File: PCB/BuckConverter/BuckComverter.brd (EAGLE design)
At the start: 65 x 60 mm, 34 parts, among them IC1 LP2950CDT-3.3

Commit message: テストパッドを追加
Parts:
- added PAD1, PAD2, PAD3, PAD4: (no value), wirepad:1,6/0,8
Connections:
- net +12V: now also PAD2.1
- net GND: now also PAD1.1
- net IC_SIG_5V: now also PAD4.1
- net VA_IN: now also PAD3.1
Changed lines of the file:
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@@
 <?xml version="1.0" encoding="utf-8"?>
 <!DOCTYPE eagle SYSTEM "eagle.dtd">
-<eagle version="7.2.0">
+<eagle version="7.5.0">
 <drawing>
 <settings>
@@
 <layers>
 <layer number="1" name="Top" color="4" fill="1" visible="yes" active="yes"/>
+<layer number="2" name="Route2" color="1" fill="3" visible="no" active="no"/>
+<layer number="3" name="Route3" color="4" fill="3" visible="no" active="no"/>
+<layer number="14" name="Route14" color="1" fill="6" visible="no" active="no"/>
+<layer number="15" name="Route15" color="4" fill="6" visible="no" active="no"/>
 <layer number="16" name="Bottom" color="1" fill="1" visible="yes" active="yes"/>
 <layer number="17" name="Pads" color="2" fill="1" visible="yes" active="yes"/>
@@
 </element>
 <element name="ZD1" library="diode" package="DO34Z7" value="BZV10" x="61.595" y="24.13" rot="R270"/>
+<element name="PAD1" library="wirepad" package="1,6/0,8" value="" x="12.7" y="38.4175"/>
+<element name="PAD2" library="wirepad" package="1,6/0,8" value="" x="13.6525" y="26.3525"/>
+<element name="PAD3" library="wirepad" package="1,6/0,8" value="" x="55.88" y="31.4325"/>
+<element name="PAD4" library="wirepad" package="1,6/0,8" value="" x="44.45" y="45.72"/>
 </elements>
 <signals>
@@
 <wire x1="23.8125" y1="26.67" x2="23.8125" y2="28.575" width="0.6096" layer="16"/>
 <wire x1="19.685" y1="32.385" x2="18.7325" y2="28.575" width="1.016" layer="16"/>
+<contactref element="PAD2" pad="1"/>
 </signal>
 <signal name="GATE_SIG">
@@
 <wire x1="48.26" y1="6.985" x2="52.705" y2="2.54" width="0.4064" layer="16"/>
 <wire x1="52.705" y1="2.54" x2="60.0075" y2="2.54" width="0.4064" layer="16"/>
+<contactref element="PAD1" pad="1"/>
 </signal>
 <signal name="N$5">
@@
 <wire x1="44.45" y1="40.64" x2="44.45" y2="45.72" width="0.4064" layer="16"/>
 <wire x1="44.45" y1="45.72" x2="49.53" y2="46.99" width="0.4064" layer="16"/>
+<contactref element="PAD4" pad="1"/>
 </signal>
 <signal name="VA_IN">
@@
 <wire x1="54.75" y1="35.68" x2="54.61" y2="36.83" width="0.254" layer="16"/>
 <wire x1="54.75" y1="35.43" x2="54.61" y2="36.83" width="0.254" layer="16"/>
-<wire x1="55.88" y1="34.29" x2="55.88" y2="27.94" width="0.4064" layer="16"/>
+<wire x1="55.88" y1="34.29" x2="55.88" y2="33.9725" width="0.4064" layer="16"/>
+<wire x1="55.88" y1="31.4325" x2="55.88" y2="27.94" width="0.4064" layer="16"/>
 <wire x1="54.75" y1="35.43" x2="55.88" y2="34.29" width="0.4064" layer="16"/>
 <wire x1="54.61" y1="46.99" x2="54.61" y2="36.83" width="0.4064" layer="16"/>
@@
 <wire x1="59.055" y1="27.94" x2="61.2775" y2="28.2575" width="0.4064" layer="16"/>
 <wire x1="61.2775" y1="28.2575" x2="61.595" y2="27.94" width="0.4064" layer="16"/>
+<contactref element="PAD3" pad="1"/>
+<wire x1="55.88" y1="31.4325" x2="55.88" y2="33.9725" width="0.4064" layer="16"/>
 </signal>
 <signal name="N$4">

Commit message: 穴径を0.8, 1.0, 1.5, 3.2mmに統一
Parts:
- added PAD5: (no value), wirepad:1,6/0,8
- moved C_PAS_OUT 0.95 mm to (23.2, 44.5)
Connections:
- net VOUT: now also PAD5.1
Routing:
- net GND: track 331.3 -> 333.0 mm
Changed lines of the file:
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@@
 <element name="C_OUT" library="rcl" package="E2,5-7" value="100uF" x="18.0975" y="45.085" rot="R270"/>
 <element name="C_PAS_IN" library="rcl" package="C3216" value="0.1uF" x="9.2075" y="32.0675" rot="MR90"/>
-<element name="C_PAS_OUT" library="rcl" package="C3216" value="0.1uF" x="24.13" y="44.45" rot="MR270"/>
+<element name="C_PAS_OUT" library="rcl" package="C3216" value="0.1uF" x="23.1775" y="44.45" rot="MR270"/>
 <element name="C_REGIN" library="rcl" package="E2,5-6" value="10u" x="5.3975" y="15.5575" rot="R270"/>
 <element name="C_REGOUT" library="rcl" package="E2,5-6" value="10u" x="20.32" y="15.5575" rot="R270"/>
@@
 <element name="PAD3" library="wirepad" package="1,6/0,8" value="" x="55.88" y="31.4325"/>
 <element name="PAD4" library="wirepad" package="1,6/0,8" value="" x="44.45" y="45.72"/>
+<element name="PAD5" library="wirepad" package="1,6/0,8" value="" x="13.335" y="53.975"/>
 </elements>
 <signals>
@@
 <wire x1="26.67" y1="36.83" x2="26.67" y2="41.91" width="1.27" layer="16"/>
 <wire x1="26.67" y1="41.91" x2="26.035" y2="42.0975" width="1.27" layer="16"/>
-<wire x1="26.035" y1="42.0975" x2="24.13" y2="43.05" width="1.27" layer="16"/>
-<wire x1="24.26" y1="42.8625" x2="24.13" y2="43.05" width="1.27" layer="16"/>
+<wire x1="26.035" y1="42.0975" x2="23.1775" y2="43.05" width="1.27" layer="16"/>
+<wire x1="24.26" y1="42.8625" x2="23.1775" y2="43.05" width="1.27" layer="16"/>
 <wire x1="24.26" y1="42.8625" x2="19.05" y2="43.18" width="1.27" layer="16"/>
 <wire x1="52.07" y1="46.99" x2="52.07" y2="36.83" width="0.4064" layer="16"/>
@@
 <vertex x="30" y="36"/>
 <vertex x="30" y="42"/>
-<vertex x="29.175" y="43.1425"/>
+<vertex x="29.4925" y="43.7775"/>
 <vertex x="4.3175" y="45.365"/>
 </polygon>
@@
 <wire x1="5.2578" y1="48.26" x2="5.055" y2="48.2389" width="0.254" layer="16"/>
 <wire x1="5.2578" y1="48.26" x2="18.0975" y2="46.355" width="1.27" layer="16"/>
-<wire x1="18.0975" y1="46.355" x2="24.13" y2="45.85" width="1.27" layer="16"/>
-<wire x1="24.13" y1="45.85" x2="28.29" y2="46.99" width="1.27" layer="16"/>
+<wire x1="18.0975" y1="46.355" x2="23.1775" y2="45.85" width="1.27" layer="16"/>
+<wire x1="23.1775" y1="45.85" x2="28.29" y2="46.99" width="1.27" layer="16"/>
 <wire x1="28.29" y1="46.99" x2="31.4325" y2="50.8" width="0.6096" layer="16"/>
 <wire x1="31.4325" y1="50.8" x2="34.29" y2="54.61" width="0.6096" layer="16"/>
@@
 <vertex x="4" y="46.0475"/>
 </polygon>
+<contactref element="PAD5" pad="1"/>
 </signal>
 <signal name="N$2">

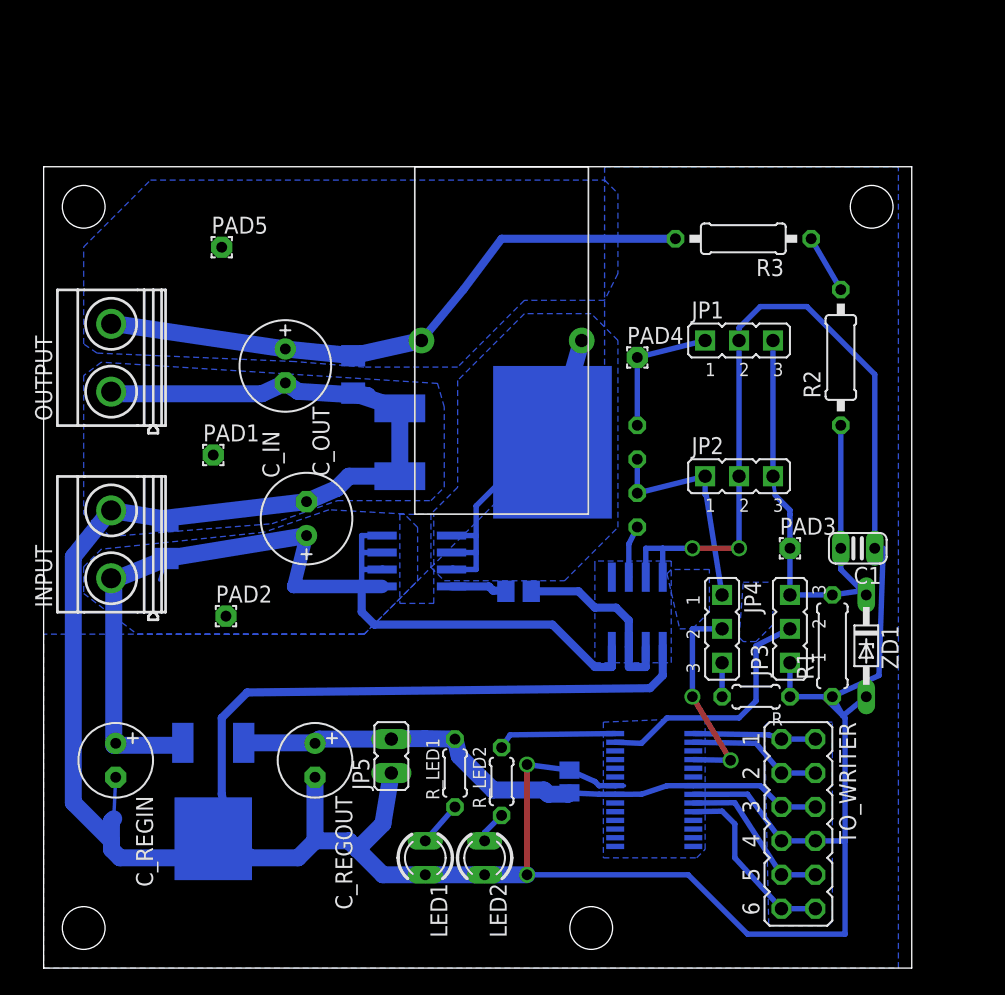
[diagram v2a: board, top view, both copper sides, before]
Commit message: 回路のミスを修正
修正内容：
レギュレータのピン配置を修正
PMOSの配線を修正
上記に伴い、パターンの再設計
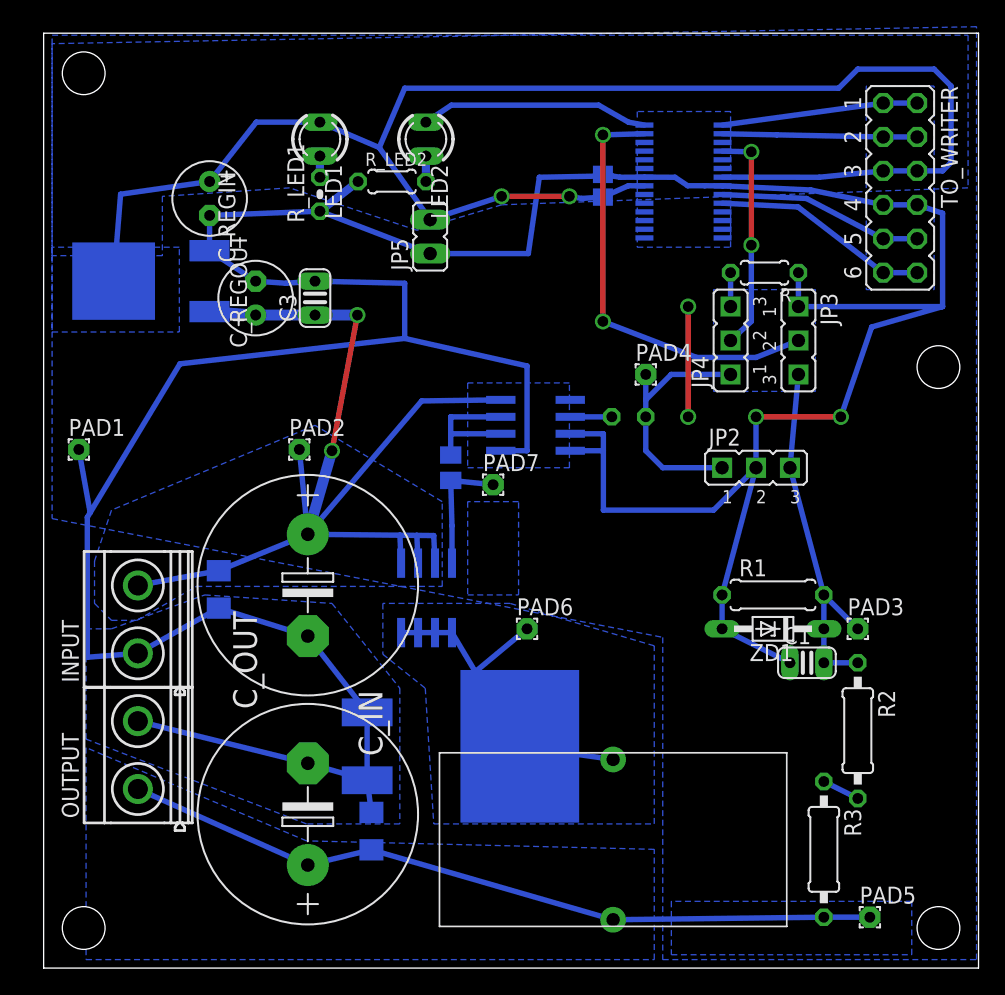
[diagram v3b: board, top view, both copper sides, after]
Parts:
- removed JP1: (no value), jumper:JP2
- removed R_5V: 150, rcl:0207/2V
- added C3: 0.1u, rcl:C025-024X044
- added PAD6, PAD7: (no value), wirepad:1,6/0,8
- C_IN, C_OUT: value 100uF -> 2200uF; device rcl:E2,5-7 -> rcl:E7,5-16
- C_REGIN, C_REGOUT: value 10u -> 100u
- IC1: value LP2950CDT-3.3 -> NPC2227DT33G; device v-reg:DPACK -> v-reg2:DPACK
- R_LED1: device rcl:0204/5 -> rcl:0204V
- moved PAD5 69.8 mm to (61.9, 3.81)
- moved LED1 54.4 mm to (20.7, 62.1)
- moved LED2 54.0 mm to (28.6, 62.1)
- moved TO_WRITER 48.2 mm to (64.1, 58.4)
- moved R3 46.1 mm to (58.4, 8.89), turned to 270 degrees
- moved R_LED2 45.7 mm to (26.1, 58.9), turned to 0 degrees
- moved U$1 45.6 mm to (47.9, 58.9)
- moved C2 44.7 mm to (41.9, 58.6)
- moved R_LED1 44.5 mm to (20.7, 57.9)
- moved C_REGOUT 42.8 mm to (12.4, 57.6)
- moved IC1 39.7 mm to (7.62, 51.4), turned to 270 degrees
- moved JP5 39.0 mm to (28.9, 54.8)
- moved L1 38.3 mm to (42.6, 9.62), turned to 270 degrees
- moved C_REGIN 36.2 mm to (15.9, 50.2), turned to 90 degrees
- moved C_PAS_OUT 34.2 mm to (24.5, 10.3), turned to 90 degrees
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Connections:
- removed net IC_SIG_5V: JP1.1, PAD4.1, R_5V.1
- removed net N$14: LED2.A, R_LED2.1
- new net N$19: DIODE.2, L1.P$1, PAD6.1, PMOS.5, PMOS.6, PMOS.7, PMOS.8
- net +12V: now also C3.1, IC1.3, INPUT.2, PMOS.1, PMOS.2, PMOS.3; no longer IC1.1, INPUT.1, PMOS.5, PMOS.6, PMOS.7, PMOS.8
- net +3V3: now also IC1.4, LED1.A; no longer IC1.3, R_LED1.2
- net GATE_SIG: now also PAD7.1
- net GND: now also C3.2, IC1.1, INPUT.1, OUTPUT.2, R_LED1.1, R_LED2.1; no longer IC1.4, INPUT.2, JP1.2, LED1.K, LED2.K, OUTPUT.1
- net IC_SIG_3.3V: now also PAD4.1; no longer R_5V.2
- net N$1: now also LED1.K, R_LED1.2; no longer DIODE.2, L1.P$1, PMOS.1, PMOS.2, PMOS.3
- net N$13: now also LED2.K; no longer U$1.14
- net N$3: now also LED2.A, U$1.14; no longer LED1.A, R_LED1.1
- net VA_IN: no longer JP1.3
- net VOUT: now also OUTPUT.1; no longer OUTPUT.2
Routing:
- net +3V3: track 50.1 -> 121.6 mm, vias 0 -> 2
- net GND: track 333.0 -> 293.6 mm
- net N$19: track 0.00 -> 25.8 mm
- net N$1: track 26.0 -> 1.59 mm
- net N$3: track 3.38 -> 17.1 mm
- net N$6: track 18.8 -> 32.5 mm, vias 0 -> 2
- net VA_IN: track 40.0 -> 28.1 mm
- net VOUT: track 46.2 -> 56.9 mm
- net IC_SIG_5V: track 10.3 -> 0.00 mm
- net N$13: track 9.02 -> 1.90 mm
- net N$9: track 9.29 -> 14.7 mm
- net GATE_SIG: track 4.22 -> 9.39 mm
- net N$10: track 10.2 -> 14.6 mm
- net N$5: track 14.7 -> 10.4 mm
- net N$11: track 12.1 -> 15.3 mm
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- added copper zone on layer 16, net +3V3
- added copper zone on layer 16, net N$19
- added copper zone on layer 16, net N$22
- removed copper zone on layer 16, net N$1
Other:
- board size 65 x 60 mm -> 70 x 70 mm

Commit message: 回路を改良
詳細:
殆どの信号線を0.016 -> 0.032 inch に変更
ゲート周りの回路の最適化
制御回路の電源ラインの最適化
一部パーツの形状を変更
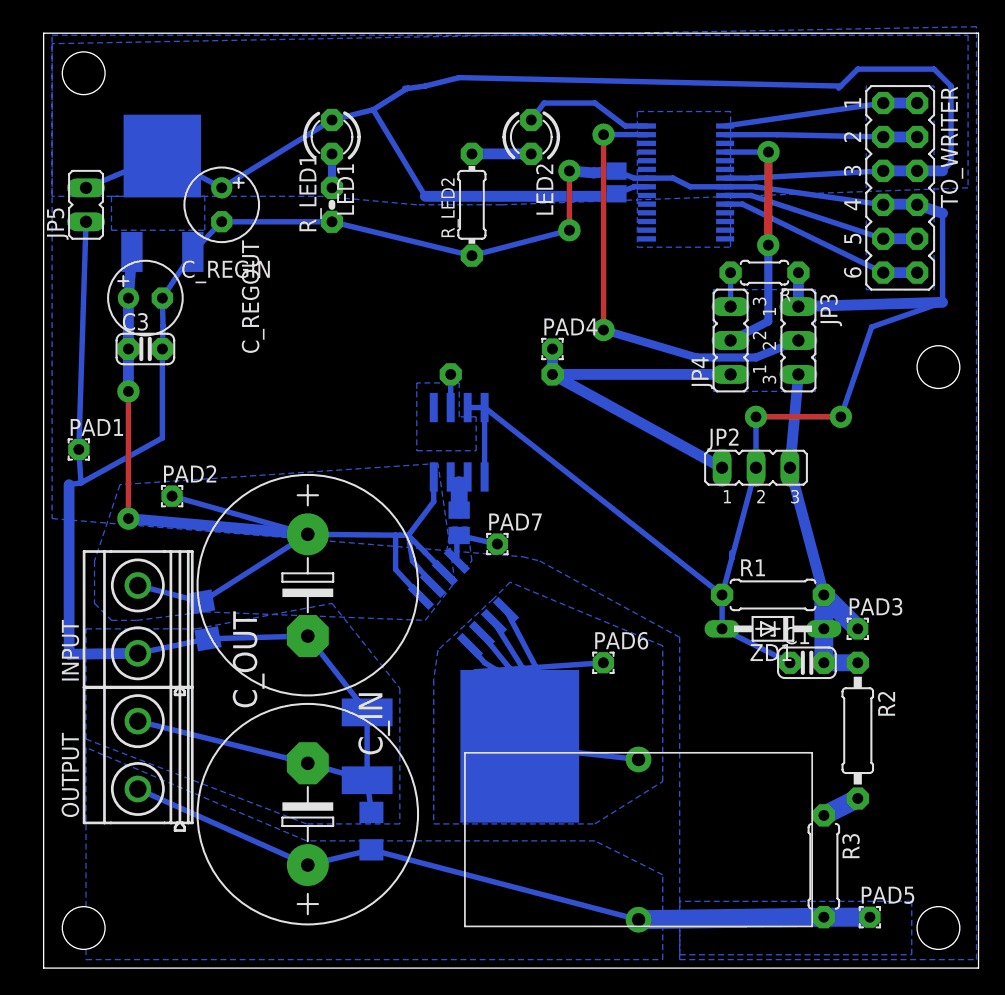
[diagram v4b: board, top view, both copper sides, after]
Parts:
- R3: device rcl:0207/10 -> rcl:0207/7
- R_3.3V: device rcl:0207/2V -> rcl:0204/7
- R_LED2: device rcl:0204/5 -> rcl:0204/7
- moved JP5 25.9 mm to (3.17, 57.1)
- moved C3 13.3 mm to (7.62, 46.4), turned to 0 degrees
- moved PAD2 10.1 mm to (9.62, 35.3)
- moved R_3.3V 10.0 mm to (34.3, 44.5)
- moved C_REGIN 8.25 mm to (7.62, 50.2), turned to 0 degrees
- moved LED2 7.89 mm to (36.5, 62.2)
- moved PAD4 7.24 mm to (38.1, 46.4)
- moved IC1 7.10 mm to (8.89, 58.4), turned to 0 degrees
- moved PAD6 6.25 mm to (41.9, 22.9)
- moved R_LED2 6.23 mm to (32.1, 57.1), turned to 90 degrees
- moved DRIVER 5.85 mm to (31.1, 39.4), turned to 180 degrees
- moved PAD7 4.46 mm to (34.0, 31.8)
- moved R_GATE 4.18 mm to (31.1, 33.3)
- moved PMOS 2.79 mm to (31.4, 27.3), turned to 135 degrees
- moved C_PAS_IN 2.54 mm to (12.1, 26.0), turned to 260 degrees
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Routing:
- net GND: track 293.6 -> 258.1 mm
- net N$19: track 25.8 -> 40.2 mm
- net IC_SIG_3.3V: track 19.1 -> 29.7 mm
- net N$3: track 17.1 -> 9.87 mm
- net N$5: track 10.4 -> 3.72 mm
- net +3V3: track 121.6 -> 117.1 mm, vias 2 -> 0
- net GATE_SIG: track 9.39 -> 5.83 mm
- net N$13: track 1.90 -> 4.45 mm
- net N$8: track 17.0 -> 19.1 mm
- net +12V: track 82.4 -> 84.5 mm
- net N$1: track 1.59 -> 2.54 mm
- net N$12: track 16.3 -> 15.6 mm
- net N$2: track 3.12 -> 2.48 mm
- net N$6: track 32.5 -> 33.0 mm
- added copper zone on layer 16, net GATE_SIG
- removed copper zone on layer 16, net N$21
